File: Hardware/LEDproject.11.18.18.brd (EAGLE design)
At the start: 36.8 x 60.6 mm, 14 parts, among them IC1 ATMEGA328-PU, Y1 16MHz

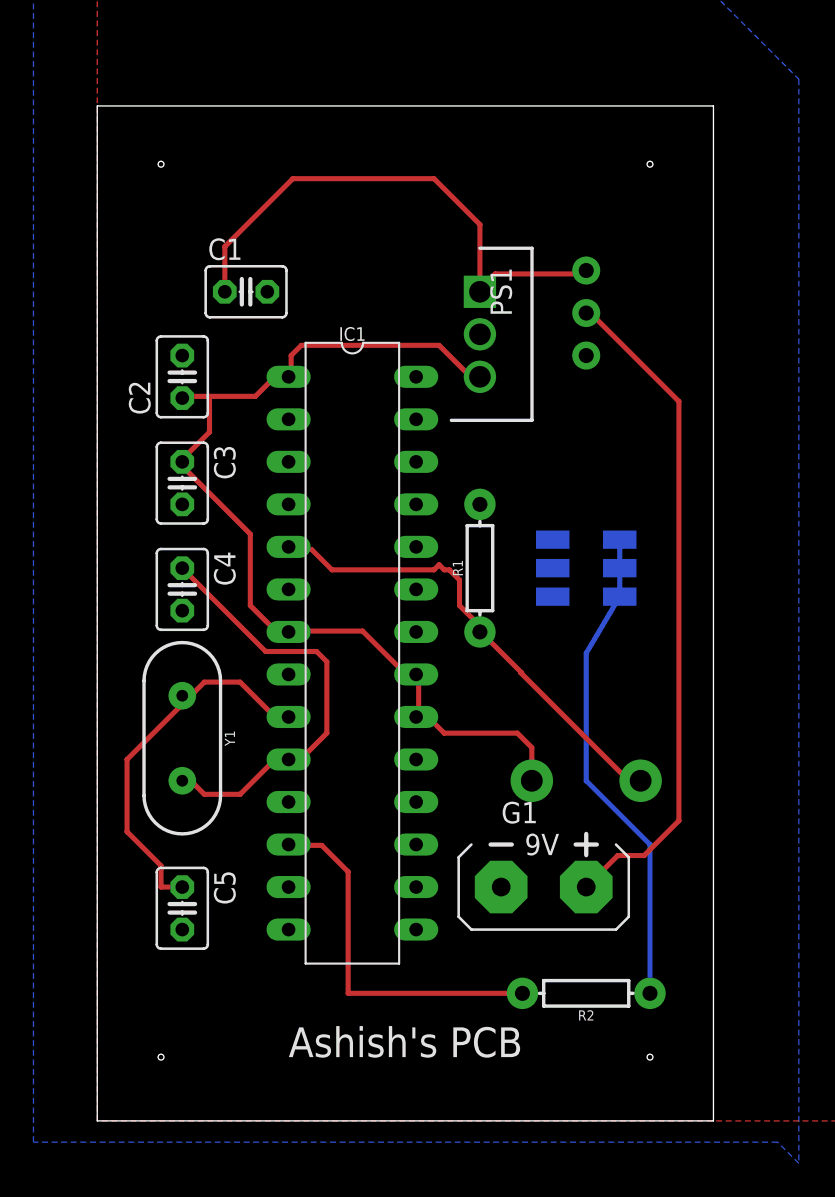
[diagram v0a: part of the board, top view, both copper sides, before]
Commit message: Adjusted PCB mounting hole, preliminary mechanical drawings
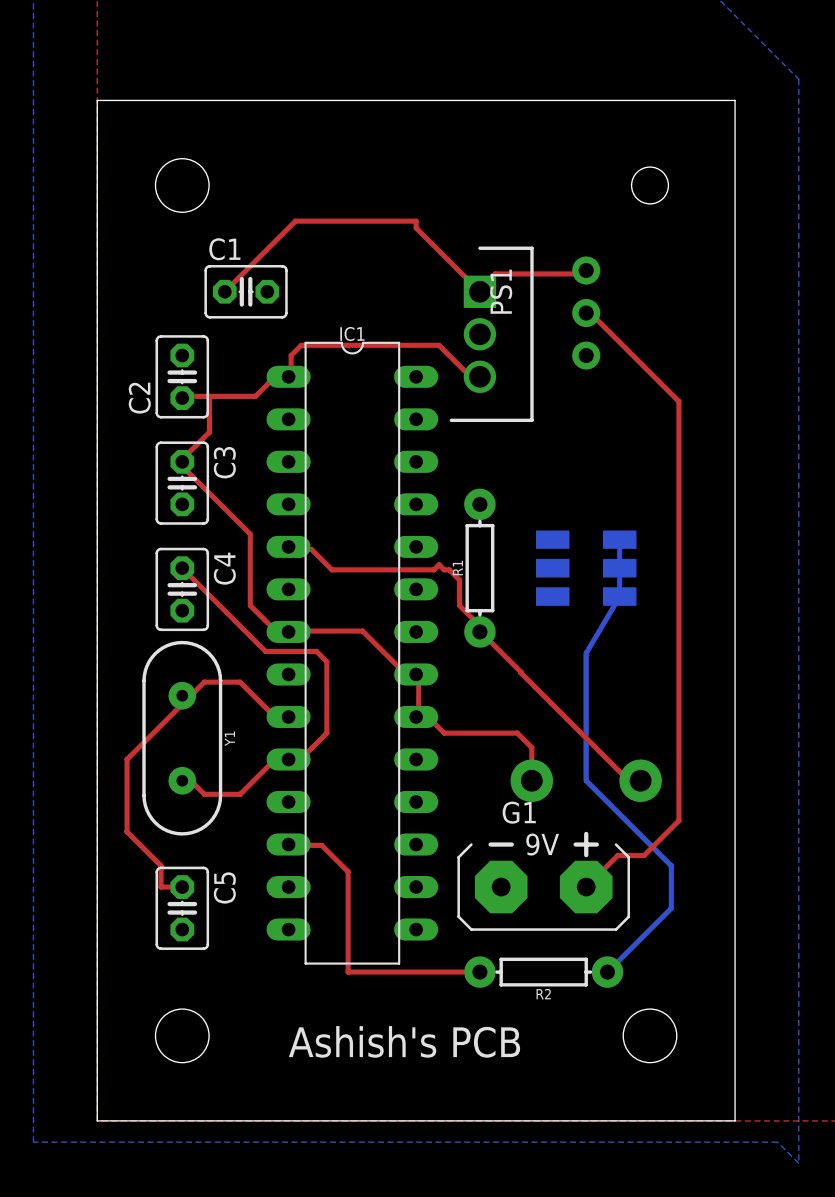
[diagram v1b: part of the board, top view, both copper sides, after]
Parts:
- moved R2 2.84 mm to (26.7, 8.89)
- renumbered SW100 to $$SW100
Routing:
- net N$5: track 31.7 -> 25.9 mm
- net N$7: track 21.9 -> 18.1 mm
- net N$4: track 29.2 -> 30.1 mm
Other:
- board size 36.8 x 60.6 mm -> 38.1 x 61 mm
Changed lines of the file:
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@@
 <setting verticaltext="up"/>
 </settings>
-<grid distance="50" unitdist="mil" unit="mil" style="lines" multiple="1" display="no" altdistance="5" altunitdist="mil" altunit="mil"/>
+<grid distance="50" unitdist="mil" unit="mil" style="lines" multiple="1" display="yes" altdistance="5" altunitdist="mil" altunit="mil"/>
 <layers>
 <layer number="1" name="Top" color="4" fill="1" visible="yes" active="yes"/>
@@
 <layer number="43" name="vRestrict" color="2" fill="10" visible="no" active="yes"/>
 <layer number="44" name="Drills" color="7" fill="1" visible="no" active="yes"/>
-<layer number="45" name="Holes" color="7" fill="1" visible="no" active="yes"/>
+<layer number="45" name="Holes" color="7" fill="1" visible="yes" active="yes"/>
 <layer number="46" name="Milling" color="3" fill="1" visible="no" active="yes"/>
 <layer number="47" name="Measures" color="7" fill="1" visible="no" active="yes"/>
@@
 <layer number="116" name="Patch_BOT" color="9" fill="4" visible="no" active="yes"/>
 <layer number="118" name="Rect_Pads" color="7" fill="1" visible="no" active="yes"/>
-<layer number="121" name="_tsilk" color="7" fill="1" visible="no" active="yes"/>
+<layer number="121" name="_tsilk" color="7" fill="1" visible="yes" active="yes"/>
 <layer number="122" name="_bsilk" color="7" fill="1" visible="no" active="yes"/>
 <layer number="123" name="tTestmark" color="7" fill="1" visible="no" active="yes"/>
@@
 <board>
 <plain>
-<wire x1="0" y1="0" x2="36.81" y2="0" width="0" layer="20"/>
-<wire x1="36.81" y1="0" x2="36.81" y2="60.63" width="0" layer="20"/>
-<wire x1="36.81" y1="60.63" x2="0" y2="60.63" width="0" layer="20"/>
-<wire x1="0" y1="60.63" x2="0" y2="0" width="0" layer="20"/>
-<hole x="3.81" y="57.15" drill="0.35"/>
-<hole x="33.02" y="57.15" drill="0.35"/>
-<hole x="33.02" y="3.81" drill="0.35"/>
-<hole x="3.81" y="3.81" drill="0.35"/>
+<wire x1="0" y1="0" x2="38.1" y2="0" width="0" layer="20"/>
+<wire x1="38.1" y1="0" x2="38.1" y2="60.96" width="0" layer="20"/>
+<wire x1="38.1" y1="60.96" x2="0" y2="60.96" width="0" layer="20"/>
+<wire x1="0" y1="60.96" x2="0" y2="0" width="0" layer="20"/>
+<hole x="5.08" y="55.88" drill="3.2"/>
+<hole x="33.02" y="55.88" drill="2.2"/>
+<hole x="33.02" y="5.08" drill="3.2"/>
+<hole x="5.08" y="5.08" drill="3.2"/>
 <text x="11.43" y="3.81" size="1.778" layer="121">Ashish's PCB</text>
 <dimension x1="0" y1="0" x2="0" y2="60.96" x3="-19.05" y3="30.48" textsize="1.778" layer="1"/>
@@
 <attribute name="NAME" x="26.67" y="51.054" size="1.27" layer="26" font="vector" rot="MR270"/>
 </element>
-<element name="SW100" library="adafruit" library_urn="urn:adsk.eagle:library:420" package="TACT_PANA-EVQ" package3d_urn="urn:adsk.eagle:package:6240957/1" value="" x="29.21" y="20.32" rot="MR0">
+<element name="$$SW100" library="adafruit" library_urn="urn:adsk.eagle:library:420" package="TACT_PANA-EVQ" package3d_urn="urn:adsk.eagle:package:6240957/1" value="" x="29.21" y="20.32" rot="MR0">
 <attribute name="NAME" x="32.253" y="22.49" size="0.8128" layer="26" ratio="18" rot="MR0"/>
 <attribute name="VALUE" x="32.226" y="17.869" size="0.4064" layer="28" ratio="10" rot="MR0"/>
@@
 <attribute name="VALUE" x="23.876" y="33.02" size="0.6096" layer="27" font="vector" ratio="20" rot="R90" align="top-center"/>
 </element>
-<element name="R2" library="SparkFun-Resistors" library_urn="urn:adsk.eagle:library:532" package="AXIAL-0.3" package3d_urn="urn:adsk.eagle:package:39658/1" value="100 Ohm" x="29.21" y="7.62" rot="R180">
-<attribute name="NAME" x="29.21" y="6.604" size="0.6096" layer="25" font="vector" ratio="20" rot="R180" align="bottom-center"/>
-<attribute name="PROD_ID" value="RES-12180" x="29.21" y="7.62" size="1.778" layer="27" rot="R180" display="off"/>
-<attribute name="VALUE" x="29.21" y="8.636" size="0.6096" layer="27" font="vector" ratio="20" rot="R180" align="top-center"/>
+<element name="R2" library="SparkFun-Resistors" library_urn="urn:adsk.eagle:library:532" package="AXIAL-0.3" package3d_urn="urn:adsk.eagle:package:39658/1" value="100 Ohm" x="26.67" y="8.89" rot="R180">
+<attribute name="NAME" x="26.67" y="7.874" size="0.6096" layer="25" font="vector" ratio="20" rot="R180" align="bottom-center"/>
+<attribute name="PROD_ID" value="RES-12180" x="26.67" y="8.89" size="1.778" layer="27" rot="R180" display="off"/>
+<attribute name="VALUE" x="26.67" y="9.906" size="0.6096" layer="27" font="vector" ratio="20" rot="R180" align="top-center"/>
 </element>
 </elements>
@@
 <contactref element="S100" pad="O"/>
 <contactref element="C1" pad="1"/>
-<wire x1="11.684" y1="56.2864" x2="7.62" y2="52.2224" width="0.3048" layer="1"/>
-<wire x1="20.1168" y1="56.2864" x2="11.684" y2="56.2864" width="0.3048" layer="1"/>
-<wire x1="22.86" y1="49.53" x2="22.86" y2="53.5432" width="0.3048" layer="1"/>
-<wire x1="22.86" y1="53.5432" x2="20.1168" y2="56.2864" width="0.3048" layer="1"/>
-<wire x1="7.62" y1="52.2224" x2="7.62" y2="49.53" width="0.3048" layer="1"/>
+<wire x1="19.05" y1="53.7464" x2="11.8364" y2="53.7464" width="0.3048" layer="1"/>
+<wire x1="7.62" y1="49.53" x2="11.8364" y2="53.7464" width="0.3048" layer="1"/>
+<wire x1="19.05" y1="53.7464" x2="19.05" y2="53.34" width="0.3048" layer="1"/>
+<wire x1="22.86" y1="49.53" x2="19.05" y2="53.34" width="0.3048" layer="1"/>
 <wire x1="28.956" y1="50.5968" x2="23.7744" y2="50.5968" width="0.3048" layer="1"/>
 <wire x1="22.86" y1="49.6824" x2="23.7744" y2="50.5968" width="0.3048" layer="1"/>
@@
 <signal name="N$6">
 <contactref element="IC1" pad="5"/>
-<contactref element="SW100" pad="P$1"/>
+<contactref element="$$SW100" pad="P$1"/>
 <contactref element="R1" pad="P$1"/>
 <wire x1="12.8016" y1="34.1376" x2="11.5824" y2="34.1376" width="0.3048" layer="1"/>
@@
 <wire x1="13.4112" y1="16.4592" x2="11.5824" y2="16.4592" width="0.3048" layer="1"/>
 <wire x1="14.986" y1="14.8844" x2="13.4112" y2="16.4592" width="0.3048" layer="1"/>
-<wire x1="14.986" y1="14.8844" x2="14.986" y2="7.62" width="0.3048" layer="1"/>
+<wire x1="14.986" y1="14.8844" x2="14.986" y2="8.89" width="0.3048" layer="1"/>
 <wire x1="11.5824" y1="16.4592" x2="11.43" y2="16.51" width="0.3048" layer="1"/>
-<wire x1="25.4" y1="7.62" x2="14.986" y2="7.62" width="0.3048" layer="1"/>
+<wire x1="22.86" y1="8.89" x2="14.986" y2="8.89" width="0.3048" layer="1"/>
 </signal>
 <signal name="+5V">
 <contactref element="PS1" pad="3"/>
-<contactref element="SW100" pad="P$2"/>
+<contactref element="$$SW100" pad="P$2"/>
 <contactref element="IC1" pad="1"/>
 <contactref element="IC1" pad="21"/>
@@
 <contactref element="LED100" pad="3"/>
 <contactref element="R2" pad="P$1"/>
-<wire x1="33.02" y1="7.62" x2="33.02" y2="16.51" width="0.3048" layer="16"/>
-<wire x1="33.02" y1="16.51" x2="29.21" y2="20.32" width="0.3048" layer="16"/>
+<wire x1="34.29" y1="15.24" x2="34.29" y2="12.7" width="0.3048" layer="16"/>
+<wire x1="34.29" y1="12.7" x2="30.48" y2="8.89" width="0.3048" layer="16"/>
+<wire x1="34.29" y1="15.24" x2="29.21" y2="20.32" width="0.3048" layer="16"/>
 <wire x1="29.21" y1="20.32" x2="29.21" y2="27.94" width="0.3048" layer="16"/>
 <wire x1="29.21" y1="27.94" x2="31.21" y2="31.32" width="0.3048" layer="16"/>
+<wire x1="31.21" y1="34.72" x2="31.21" y2="33.02" width="0.3048" layer="16"/>
 <wire x1="31.21" y1="31.32" x2="31.21" y2="33.02" width="0.3048" layer="16"/>
-<wire x1="31.21" y1="34.72" x2="31.21" y2="33.02" width="0.3048" layer="16"/>
 </signal>
 </signals>
